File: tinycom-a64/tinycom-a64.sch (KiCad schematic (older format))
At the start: 25 parts, among them P1 CONN_02X10, P2 CONN_02X10, U1 AllWinner-A64(FBGA396), U2 H5TQG63BFR/FBGA96

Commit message: route
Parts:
- added C? (x2): C_Small, Capacitors_SMD:C_0603, symbol C_Small
- added Y1: Crystal, Crystals:crystal_FA238-TSX3225, symbol Crystal
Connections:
- net GND: now also C?.2, C?.2
- net SDC0_CLK: now also U1.AC8 (PF2/SDC0-CLK/UART0-TX)
- net SDC0_CMD: now also U1.W9 (PF3/SDC0-CMD/JTAG-DO1)
- net SDC0_D0: now also U1.W13 (PF1/SDC0-D0/JTAG-DI1)
- net SDC0_D1: now also U1.AB10 (PF0/SDC0-D1/JTAG-MS1)
- net SDC0_D2: now also U1.AB9 (PF5/SDC0-D2/JTAG-CK1)
- net SDC0_D3: now also U1.AB6 (PF4/SDC0-D3/UART0-RX)
- net UD0_N: now also U1.B22 (USB0-DM)
- net UD0_P: now also U1.A22 (USB0-DP)
- net UD2_N: now also U1.C22 (USB1-DM)
- net UD2_P: now also U1.B23 (USB1-DP)
- net at U1.K22 (X24MI): now also C?.1, Y1.1
- net at U1.K23 (X24MO): now also C?.1, Y1.2
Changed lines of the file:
@@
 $EndComp
 $Comp
-L GND #PWR4
+L GND #PWR01
 U 1 1 563E445F
 P 17800 6150
-F 0 "#PWR4" H 17800 5900 50  0001 C CNN
+F 0 "#PWR01" H 17800 5900 50  0001 C CNN
 F 1 "GND" H 17800 6000 50  0000 C CNN
 F 2 "" H 17800 6150 60  0000 C CNN
@@
 SCK_P
 $Comp
-L GND #PWR3
+L GND #PWR02
 U 1 1 563ECE56
 P 14950 850
-F 0 "#PWR3" H 14950 600 50  0001 C CNN
+F 0 "#PWR02" H 14950 600 50  0001 C CNN
 F 1 "GND" H 14950 700 50  0000 C CNN
 F 2 "" H 14950 850 60  0000 C CNN
@@
 $EndComp
 $Comp
-L GND #PWR1
+L GND #PWR03
 U 1 1 563EDF36
 P 13600 5900
-F 0 "#PWR1" H 13600 5650 50  0001 C CNN
+F 0 "#PWR03" H 13600 5650 50  0001 C CNN
 F 1 "GND" H 13600 5750 50  0000 C CNN
 F 2 "" H 13600 5900 60  0000 C CNN
@@
 $EndComp
 $Comp
-L GND #PWR2
+L GND #PWR04
 U 1 1 563EE398
 P 14350 5150
-F 0 "#PWR2" H 14350 4900 50  0001 C CNN
+F 0 "#PWR04" H 14350 4900 50  0001 C CNN
 F 1 "GND" H 14350 5000 50  0000 C CNN
 F 2 "" H 14350 5150 60  0000 C CNN
@@
 VCC_33
 $Comp
-L GND #PWR5
+L GND #PWR05
 U 1 1 56440C85
 P 19500 8700
-F 0 "#PWR5" H 19500 8450 50  0001 C CNN
+F 0 "#PWR05" H 19500 8450 50  0001 C CNN
 F 1 "GND" H 19500 8550 50  0000 C CNN
 F 2 "" H 19500 8700 60  0000 C CNN
@@
 $EndComp
 $Comp
-L GND #PWR7
+L GND #PWR06
 U 1 1 56441E51
 P 20300 8700
-F 0 "#PWR7" H 20300 8450 50  0001 C CNN
+F 0 "#PWR06" H 20300 8450 50  0001 C CNN
 F 1 "GND" H 20300 8550 50  0000 C CNN
 F 2 "" H 20300 8700 60  0000 C CNN
@@
 $EndComp
 $Comp
-L GND #PWR9
+L GND #PWR07
 U 1 1 564426D1
 P 20950 8700
-F 0 "#PWR9" H 20950 8450 50  0001 C CNN
+F 0 "#PWR07" H 20950 8450 50  0001 C CNN
 F 1 "GND" H 20950 8550 50  0000 C CNN
 F 2 "" H 20950 8700 60  0000 C CNN
@@
 HSDA
 $Comp
-L GND #PWR6
+L GND #PWR08
 U 1 1 56627185
 P 19800 9450
-F 0 "#PWR6" H 19800 9200 50  0001 C CNN
+F 0 "#PWR08" H 19800 9200 50  0001 C CNN
 F 1 "GND" H 19800 9300 50  0000 C CNN
 F 2 "" H 19800 9450 50  0000 C CNN
@@
 UART0_TX
 $Comp
-L GND #PWR8
+L GND #PWR09
 U 1 1 566278FC
 P 20500 10550
-F 0 "#PWR8" H 20500 10300 50  0001 C CNN
+F 0 "#PWR09" H 20500 10300 50  0001 C CNN
 F 1 "GND" H 20500 10400 50  0000 C CNN
 F 2 "" H 20500 10550 50  0000 C CNN
@@
 Text GLabel 11450 6250 2    60   Input ~ 0
 SVREF
+Text GLabel 7950 1800 2    60   Input ~ 0
+SDC0_D1
+Text GLabel 7950 1900 2    60   Input ~ 0
+SDC0_D0
+Text GLabel 7950 2000 2    60   Input ~ 0
+SDC0_CLK
+Text GLabel 7950 2100 2    60   Input ~ 0
+SDC0_CMD
+Text GLabel 7950 2200 2    60   Input ~ 0
+SDC0_D3
+Text GLabel 7950 2300 2    60   Input ~ 0
+SDC0_D2
+Text GLabel 6350 7900 2    60   Input ~ 0
+UD0_N
+Text GLabel 6350 8000 2    60   Input ~ 0
+UD0_P
+Text GLabel 6350 8100 2    60   Input ~ 0
+UD2_N
+Text GLabel 6350 8200 2    60   Input ~ 0
+UD2_P
+Wire Wire Line
+	1650 2050 1650 2100
+Wire Wire Line
+	1050 1850 1450 1850
+Wire Wire Line
+	1450 1850 1450 2000
+Wire Wire Line
+	1450 2000 1650 2000
+$Comp
+L Crystal Y1
+U 1 1 5669666E
+P 1200 2050
+F 0 "Y1" H 1200 2200 50  0000 C CNN
+F 1 "Crystal" H 1200 1900 50  0000 C CNN
+F 2 "Crystals:crystal_FA238-TSX3225" H 1200 2050 50  0000 C CNN
+F 3 "" H 1200 2050 50  0000 C CNN
+	1    1200 2050
+	-1   0    0    -1
+$EndComp
+Wire Wire Line
+	1650 2050 1350 2050
+Connection ~ 1050 2050
+Wire Wire Line
+	1350 2050 1350 2200
+Wire Wire Line
+	1050 1850 1050 2200
+$Comp
+L C_Small C?
+U 1 1 56694D06
+P 1050 2300
+F 0 "C?" H 1060 2370 50  0000 L CNN
+F 1 "C_Small" H 1060 2220 50  0000 L CNN
+F 2 "Capacitors_SMD:C_0603" H 1050 2300 60  0001 C CNN
+F 3 "" H 1050 2300 60  0000 C CNN
+	1    1050 2300
+	1    0    0    -1
+$EndComp
+$Comp
+L C_Small C?
+U 1 1 566951D3
+P 1350 2300
+F 0 "C?" H 1360 2370 50  0000 L CNN
+F 1 "C_Small" H 1360 2220 50  0000 L CNN
+F 2 "Capacitors_SMD:C_0603" H 1350 2300 60  0001 C CNN
+F 3 "" H 1350 2300 60  0000 C CNN
+	1    1350 2300
+	1    0    0    -1
+$EndComp
+$Comp
+L GND #PWR?
+U 1 1 5669523B
+P 1050 2400
+F 0 "#PWR?" H 1050 2150 50  0001 C CNN
+F 1 "GND" H 1050 2250 50  0000 C CNN
+F 2 "" H 1050 2400 50  0000 C CNN
+F 3 "" H 1050 2400 50  0000 C CNN
+	1    1050 2400
+	1    0    0    -1
+$EndComp
+$Comp
+L GND #PWR?
+U 1 1 566952BF
+P 1350 2400
+F 0 "#PWR?" H 1350 2150 50  0001 C CNN
+F 1 "GND" H 1350 2250 50  0000 C CNN
+F 2 "" H 1350 2400 50  0000 C CNN
+F 3 "" H 1350 2400 50  0000 C CNN
+	1    1350 2400
+	1    0    0    -1
+$EndComp
 $EndSCHEMATC

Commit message: xxx
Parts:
- gave numbers to parts that had none: 2
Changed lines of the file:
@@
 $EndComp
 $Comp
-L GND #PWR01
+L GND #PWR6
 U 1 1 563E445F
 P 17800 6150
-F 0 "#PWR01" H 17800 5900 50  0001 C CNN
+F 0 "#PWR6" H 17800 5900 50  0001 C CNN
 F 1 "GND" H 17800 6000 50  0000 C CNN
 F 2 "" H 17800 6150 60  0000 C CNN
@@
 SCK_P
 $Comp
-L GND #PWR02
+L GND #PWR5
 U 1 1 563ECE56
 P 14950 850
-F 0 "#PWR02" H 14950 600 50  0001 C CNN
+F 0 "#PWR5" H 14950 600 50  0001 C CNN
 F 1 "GND" H 14950 700 50  0000 C CNN
 F 2 "" H 14950 850 60  0000 C CNN
@@
 $EndComp
 $Comp
-L GND #PWR03
+L GND #PWR3
 U 1 1 563EDF36
 P 13600 5900
-F 0 "#PWR03" H 13600 5650 50  0001 C CNN
+F 0 "#PWR3" H 13600 5650 50  0001 C CNN
 F 1 "GND" H 13600 5750 50  0000 C CNN
 F 2 "" H 13600 5900 60  0000 C CNN
@@
 $EndComp
 $Comp
-L GND #PWR04
+L GND #PWR4
 U 1 1 563EE398
 P 14350 5150
-F 0 "#PWR04" H 14350 4900 50  0001 C CNN
+F 0 "#PWR4" H 14350 4900 50  0001 C CNN
 F 1 "GND" H 14350 5000 50  0000 C CNN
 F 2 "" H 14350 5150 60  0000 C CNN
@@
 VCC_33
 $Comp
-L GND #PWR05
+L GND #PWR7
 U 1 1 56440C85
 P 19500 8700
-F 0 "#PWR05" H 19500 8450 50  0001 C CNN
+F 0 "#PWR7" H 19500 8450 50  0001 C CNN
 F 1 "GND" H 19500 8550 50  0000 C CNN
 F 2 "" H 19500 8700 60  0000 C CNN
@@
 $EndComp
 $Comp
-L GND #PWR06
+L GND #PWR9
 U 1 1 56441E51
 P 20300 8700
-F 0 "#PWR06" H 20300 8450 50  0001 C CNN
+F 0 "#PWR9" H 20300 8450 50  0001 C CNN
 F 1 "GND" H 20300 8550 50  0000 C CNN
 F 2 "" H 20300 8700 60  0000 C CNN
@@
 $EndComp
 $Comp
-L GND #PWR07
+L GND #PWR11
 U 1 1 564426D1
 P 20950 8700
-F 0 "#PWR07" H 20950 8450 50  0001 C CNN
+F 0 "#PWR11" H 20950 8450 50  0001 C CNN
 F 1 "GND" H 20950 8550 50  0000 C CNN
 F 2 "" H 20950 8700 60  0000 C CNN
@@
 HSDA
 $Comp
-L GND #PWR08
+L GND #PWR8
 U 1 1 56627185
 P 19800 9450
-F 0 "#PWR08" H 19800 9200 50  0001 C CNN
+F 0 "#PWR8" H 19800 9200 50  0001 C CNN
 F 1 "GND" H 19800 9300 50  0000 C CNN
 F 2 "" H 19800 9450 50  0000 C CNN
@@
 UART0_TX
 $Comp
-L GND #PWR09
+L GND #PWR10
 U 1 1 566278FC
 P 20500 10550
-F 0 "#PWR09" H 20500 10300 50  0001 C CNN
+F 0 "#PWR10" H 20500 10300 50  0001 C CNN
 F 1 "GND" H 20500 10400 50  0000 C CNN
 F 2 "" H 20500 10550 50  0000 C CNN
@@
 	1050 1850 1050 2200
 $Comp
-L C_Small C?
+L C_Small C1
 U 1 1 56694D06
 P 1050 2300
-F 0 "C?" H 1060 2370 50  0000 L CNN
+F 0 "C1" H 1060 2370 50  0000 L CNN
 F 1 "C_Small" H 1060 2220 50  0000 L CNN
 F 2 "Capacitors_SMD:C_0603" H 1050 2300 60  0001 C CNN
@@
 $EndComp
 $Comp
-L C_Small C?
+L C_Small C2
 U 1 1 566951D3
 P 1350 2300
-F 0 "C?" H 1360 2370 50  0000 L CNN
+F 0 "C2" H 1360 2370 50  0000 L CNN
 F 1 "C_Small" H 1360 2220 50  0000 L CNN
 F 2 "Capacitors_SMD:C_0603" H 1350 2300 60  0001 C CNN
@@
 $EndComp
 $Comp
-L GND #PWR?
+L GND #PWR1
 U 1 1 5669523B
 P 1050 2400
-F 0 "#PWR?" H 1050 2150 50  0001 C CNN
+F 0 "#PWR1" H 1050 2150 50  0001 C CNN
 F 1 "GND" H 1050 2250 50  0000 C CNN
 F 2 "" H 1050 2400 50  0000 C CNN
@@
 $EndComp
 $Comp
-L GND #PWR?
+L GND #PWR2
 U 1 1 566952BF
 P 1350 2400
-F 0 "#PWR?" H 1350 2150 50  0001 C CNN
+F 0 "#PWR2" H 1350 2150 50  0001 C CNN
 F 1 "GND" H 1350 2250 50  0000 C CNN
 F 2 "" H 1350 2400 50  0000 C CNN

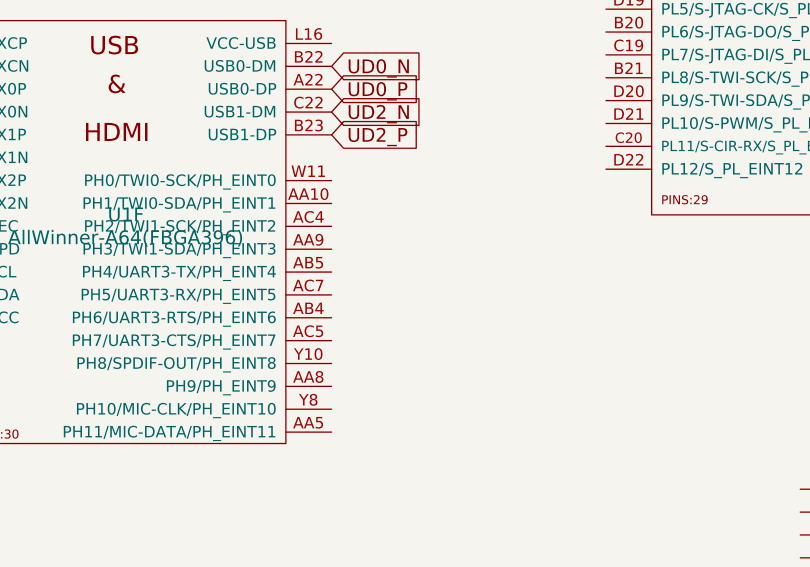
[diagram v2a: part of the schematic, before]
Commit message: route uart
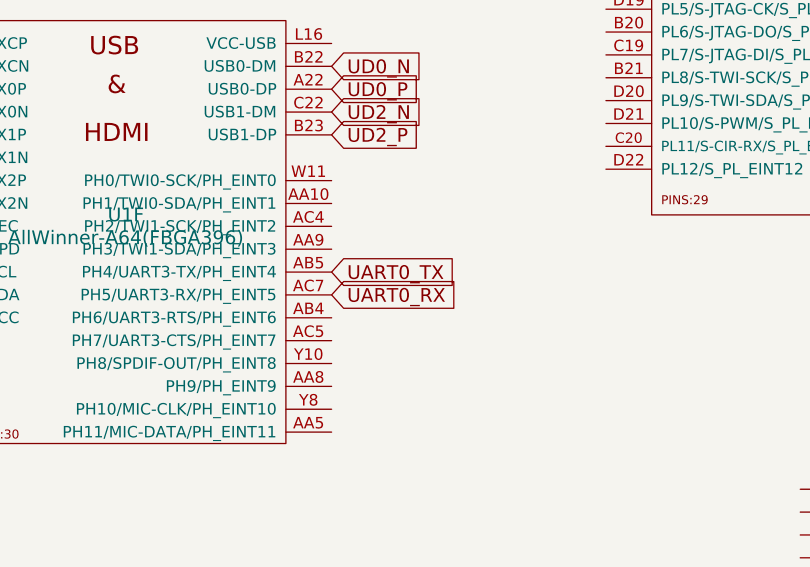
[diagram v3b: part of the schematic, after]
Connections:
- net UART0_RX: now also U1.AC7 (PH5/UART3-RX/PH_EINT5)
- net UART0_TX: now also U1.AB5 (PH4/UART3-TX/PH_EINT4)
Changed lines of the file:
@@
 $EndComp
 $Comp
-L GND #PWR6
+L GND #PWR01
 U 1 1 563E445F
 P 17800 6150
-F 0 "#PWR6" H 17800 5900 50  0001 C CNN
+F 0 "#PWR01" H 17800 5900 50  0001 C CNN
 F 1 "GND" H 17800 6000 50  0000 C CNN
 F 2 "" H 17800 6150 60  0000 C CNN
@@
 SCK_P
 $Comp
-L GND #PWR5
+L GND #PWR02
 U 1 1 563ECE56
 P 14950 850
-F 0 "#PWR5" H 14950 600 50  0001 C CNN
+F 0 "#PWR02" H 14950 600 50  0001 C CNN
 F 1 "GND" H 14950 700 50  0000 C CNN
 F 2 "" H 14950 850 60  0000 C CNN
@@
 $EndComp
 $Comp
-L GND #PWR3
+L GND #PWR03
 U 1 1 563EDF36
 P 13600 5900
-F 0 "#PWR3" H 13600 5650 50  0001 C CNN
+F 0 "#PWR03" H 13600 5650 50  0001 C CNN
 F 1 "GND" H 13600 5750 50  0000 C CNN
 F 2 "" H 13600 5900 60  0000 C CNN
@@
 $EndComp
 $Comp
-L GND #PWR4
+L GND #PWR04
 U 1 1 563EE398
 P 14350 5150
-F 0 "#PWR4" H 14350 4900 50  0001 C CNN
+F 0 "#PWR04" H 14350 4900 50  0001 C CNN
 F 1 "GND" H 14350 5000 50  0000 C CNN
 F 2 "" H 14350 5150 60  0000 C CNN
@@
 VCC_33
 $Comp
-L GND #PWR7
+L GND #PWR05
 U 1 1 56440C85
 P 19500 8700
-F 0 "#PWR7" H 19500 8450 50  0001 C CNN
+F 0 "#PWR05" H 19500 8450 50  0001 C CNN
 F 1 "GND" H 19500 8550 50  0000 C CNN
 F 2 "" H 19500 8700 60  0000 C CNN
@@
 $EndComp
 $Comp
-L GND #PWR9
+L GND #PWR06
 U 1 1 56441E51
 P 20300 8700
-F 0 "#PWR9" H 20300 8450 50  0001 C CNN
+F 0 "#PWR06" H 20300 8450 50  0001 C CNN
 F 1 "GND" H 20300 8550 50  0000 C CNN
 F 2 "" H 20300 8700 60  0000 C CNN
@@
 $EndComp
 $Comp
-L GND #PWR11
+L GND #PWR07
 U 1 1 564426D1
 P 20950 8700
-F 0 "#PWR11" H 20950 8450 50  0001 C CNN
+F 0 "#PWR07" H 20950 8450 50  0001 C CNN
 F 1 "GND" H 20950 8550 50  0000 C CNN
 F 2 "" H 20950 8700 60  0000 C CNN
@@
 HSDA
 $Comp
-L GND #PWR8
+L GND #PWR08
 U 1 1 56627185
 P 19800 9450
-F 0 "#PWR8" H 19800 9200 50  0001 C CNN
+F 0 "#PWR08" H 19800 9200 50  0001 C CNN
 F 1 "GND" H 19800 9300 50  0000 C CNN
 F 2 "" H 19800 9450 50  0000 C CNN
@@
 UART0_TX
 $Comp
-L GND #PWR10
+L GND #PWR09
 U 1 1 566278FC
 P 20500 10550
-F 0 "#PWR10" H 20500 10300 50  0001 C CNN
+F 0 "#PWR09" H 20500 10300 50  0001 C CNN
 F 1 "GND" H 20500 10400 50  0000 C CNN
 F 2 "" H 20500 10550 50  0000 C CNN
@@
 $EndComp
 $Comp
-L GND #PWR1
+L GND #PWR010
 U 1 1 5669523B
 P 1050 2400
-F 0 "#PWR1" H 1050 2150 50  0001 C CNN
+F 0 "#PWR010" H 1050 2150 50  0001 C CNN
 F 1 "GND" H 1050 2250 50  0000 C CNN
 F 2 "" H 1050 2400 50  0000 C CNN
@@
 $EndComp
 $Comp
-L GND #PWR2
+L GND #PWR011
 U 1 1 566952BF
 P 1350 2400
-F 0 "#PWR2" H 1350 2150 50  0001 C CNN
+F 0 "#PWR011" H 1350 2150 50  0001 C CNN
 F 1 "GND" H 1350 2250 50  0000 C CNN
 F 2 "" H 1350 2400 50  0000 C CNN
@@
 	1    0    0    -1
 $EndComp
+Text GLabel 6350 8800 2    60   Input ~ 0
+UART0_TX
+Text GLabel 6350 8900 2    60   Input ~ 0
+UART0_RX
 $EndSCHEMATC

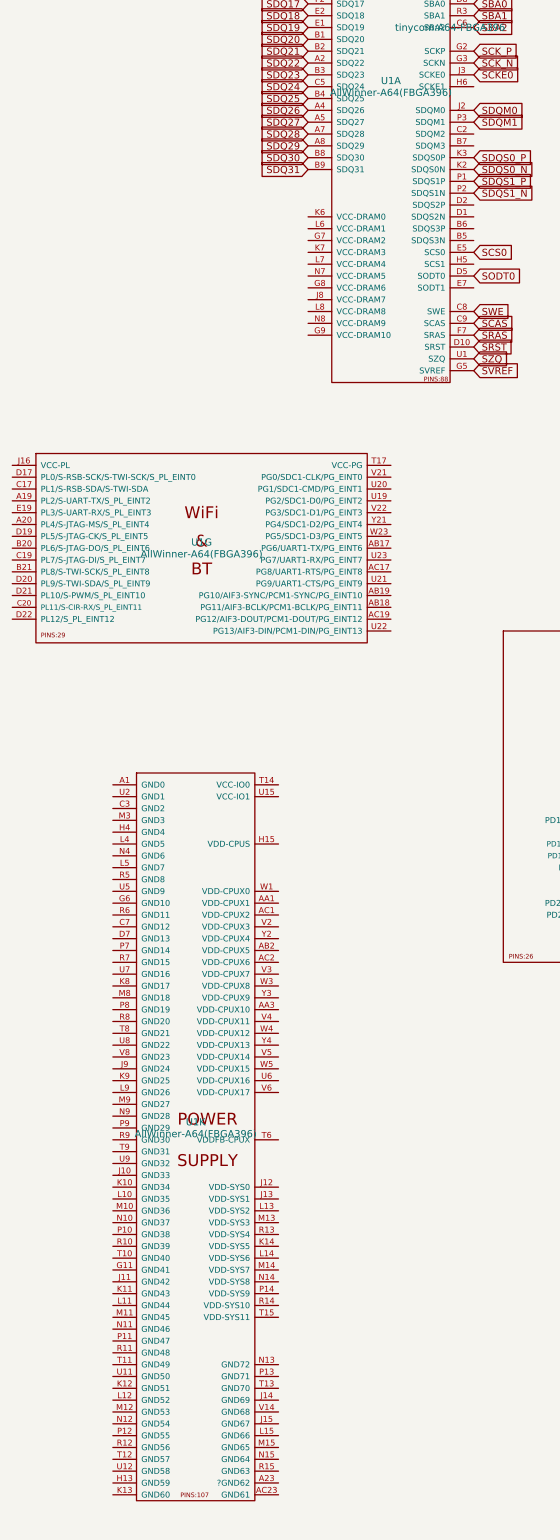
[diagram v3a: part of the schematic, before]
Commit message: route ddr power
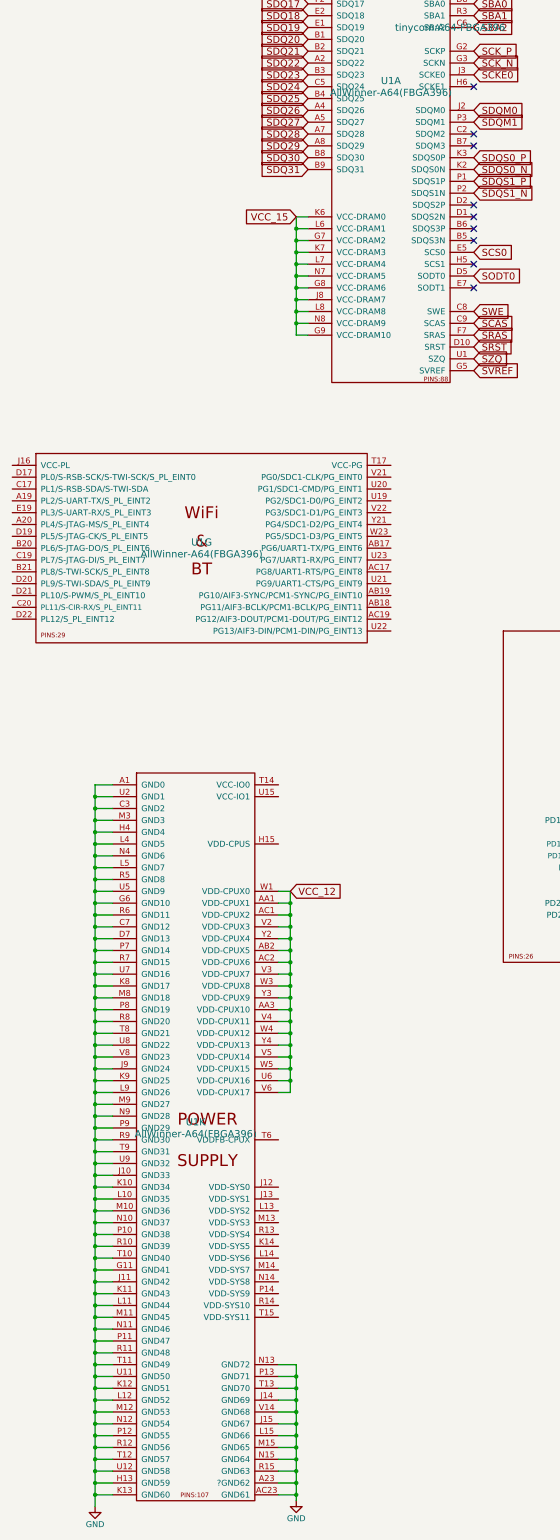
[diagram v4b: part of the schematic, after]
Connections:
- net GND: now also U1.A1 (GND0), U1.A23 (?GND62), U1.AC23 (GND61), U1.C3 (GND2), U1.C7 (GND12), U1.D7 (GND13), U1.G11 (GND41), U1.G6 (GND10), U1.H13 (GND59), U1.H4 (GND4), U1.J10 (GND33), U1.J11 (GND42), U1.J14 (GND69), U1.J15 (GND67), U1.J9 (GND24), U1.K10 (GND34), U1.K11 (GND43), U1.K12 (GND51), U1.K13 (GND60), U1.K8 (GND17), U1.K9 (GND25), U1.L10 (GND35), U1.L11 (GND44), U1.L12 (GND52), U1.L15 (GND66), U1.L4 (GND5), U1.L5 (GND7), U1.L9 (GND26), U1.M10 (GND36), U1.M11 (GND45), U1.M12 (GND53), U1.M15 (GND65), U1.M3 (GND3), U1.M8 (GND18), U1.M9 (GND27), U1.N10 (GND37), U1.N11 (GND46), U1.N12 (GND54), U1.N13 (GND72), U1.N15 (GND64), U1.N4 (GND6), U1.N9 (GND28), U1.P10 (GND38), U1.P11 (GND47), U1.P12 (GND55), U1.P13 (GND71), U1.P7 (GND14), U1.P8 (GND19), U1.P9 (GND29), U1.R10 (GND39), U1.R11 (GND48), U1.R12 (GND56), U1.R15 (GND63), U1.R5 (GND8), U1.R6 (GND11), U1.R7 (GND15), U1.R8 (GND20), U1.R9 (GND30), U1.T10 (GND40), U1.T11 (GND49), U1.T12 (GND57), U1.T13 (GND70), U1.T8 (GND21), U1.T9 (GND31), U1.U11 (GND50), U1.U12 (GND58), U1.U2 (GND1), U1.U5 (GND9), U1.U7 (GND16), U1.U8 (GND22), U1.U9 (GND32), U1.V14 (GND68), U1.V8 (GND23)
- net VCC_12: now also U1.AA1 (VDD-CPUX1), U1.AA3 (VDD-CPUX10), U1.AB2 (VDD-CPUX5), U1.AC1 (VDD-CPUX2), U1.AC2 (VDD-CPUX6), U1.U6 (VDD-CPUX16), U1.V2 (VDD-CPUX3), U1.V3 (VDD-CPUX7), U1.V4 (VDD-CPUX11), U1.V5 (VDD-CPUX14), U1.V6 (VDD-CPUX17), U1.W1 (VDD-CPUX0), U1.W3 (VDD-CPUX8), U1.W4 (VDD-CPUX12), U1.W5 (VDD-CPUX15), U1.Y2 (VDD-CPUX4), U1.Y3 (VDD-CPUX9), U1.Y4 (VDD-CPUX13)
- net VCC_15: now also U1.G7 (VCC-DRAM2), U1.G8 (VCC-DRAM6), U1.G9 (VCC-DRAM10), U1.J8 (VCC-DRAM7), U1.K6 (VCC-DRAM0), U1.K7 (VCC-DRAM3), U1.L6 (VCC-DRAM1), U1.L7 (VCC-DRAM4), U1.L8 (VCC-DRAM8), U1.N7 (VCC-DRAM5), U1.N8 (VCC-DRAM9)
- no-connect marks 5 -> 14

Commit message: route
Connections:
- net VCC_12: now also U1.J12 (VDD-SYS0), U1.J13 (VDD-SYS1), U1.K14 (VDD-SYS5), U1.L13 (VDD-SYS2), U1.L14 (VDD-SYS6), U1.M13 (VDD-SYS3), U1.M14 (VDD-SYS7), U1.N14 (VDD-SYS8), U1.P14 (VDD-SYS9), U1.R13 (VDD-SYS4), U1.R14 (VDD-SYS10), U1.T15 (VDD-SYS11)
- net VCC_33: now also U1.L16 (VCC-USB)
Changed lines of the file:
@@
 UART0_RX
 $Comp
-L GND #PWR?
+L GND #PWR012
 U 1 1 56696AA6
 P 8250 15850
-F 0 "#PWR?" H 8250 15600 50  0001 C CNN
+F 0 "#PWR012" H 8250 15600 50  0001 C CNN
 F 1 "GND" H 8250 15700 50  0000 C CNN
 F 2 "" H 8250 15850 50  0000 C CNN
@@
 Connection ~ 9900 12250
 $Comp
-L GND #PWR?
+L GND #PWR013
 U 1 1 5669EC55
 P 9950 15800
-F 0 "#PWR?" H 9950 15550 50  0001 C CNN
+F 0 "#PWR013" H 9950 15550 50  0001 C CNN
 F 1 "GND" H 9950 15650 50  0000 C CNN
 F 2 "" H 9950 15800 50  0000 C CNN
@@
 NoConn ~ 11450 5350
 NoConn ~ 11450 5550
+Wire Wire Line
+	9800 13150 9900 13150
+Wire Wire Line
+	9900 13150 9900 14250
+Wire Wire Line
+	9900 14250 9800 14250
+Wire Wire Line
+	9800 13250 9900 13250
+Connection ~ 9900 13250
+Wire Wire Line
+	9800 13350 9900 13350
+Connection ~ 9900 13350
+Wire Wire Line
+	9800 13450 9900 13450
+Connection ~ 9900 13450
+Wire Wire Line
+	9800 13550 9900 13550
+Connection ~ 9900 13550
+Wire Wire Line
+	9800 13650 9900 13650
+Connection ~ 9900 13650
+Wire Wire Line
+	9800 13750 9900 13750
+Connection ~ 9900 13750
+Wire Wire Line
+	9800 13850 9900 13850
+Connection ~ 9900 13850
+Wire Wire Line
+	9800 13950 9900 13950
+Connection ~ 9900 13950
+Wire Wire Line
+	9800 14050 9900 14050
+Connection ~ 9900 14050
+Wire Wire Line
+	9800 14150 9900 14150
+Connection ~ 9900 14150
+Text GLabel 9900 13150 2    60   Input ~ 0
+VCC_12
+Text GLabel 6350 7800 2    60   Input ~ 0
+VCC_33
 $EndSCHEMATC

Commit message: reroute, escape bga
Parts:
- C1, C2: value C_Small -> 33pF
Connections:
- net VCC_12 is gone; now on net VCC_11: C14.1, C15.1, C20.1, C22.1, C6.1, P2.3 (P3), U1.AA1 (VDD-CPUX1), U1.AA3 (VDD-CPUX10), U1.AB2 (VDD-CPUX5), U1.AC1 (VDD-CPUX2), U1.AC2 (VDD-CPUX6), U1.J12 (VDD-SYS0), U1.J13 (VDD-SYS1), U1.K14 (VDD-SYS5), U1.L13 (VDD-SYS2), U1.L14 (VDD-SYS6), U1.M13 (VDD-SYS3), U1.M14 (VDD-SYS7), U1.N14 (VDD-SYS8), U1.P14 (VDD-SYS9), U1.R13 (VDD-SYS4), U1.R14 (VDD-SYS10), U1.T15 (VDD-SYS11), U1.U6 (VDD-CPUX16), U1.V2 (VDD-CPUX3), U1.V3 (VDD-CPUX7), U1.V4 (VDD-CPUX11), U1.V5 (VDD-CPUX14), U1.V6 (VDD-CPUX17), U1.W1 (VDD-CPUX0), U1.W3 (VDD-CPUX8), U1.W4 (VDD-CPUX12), U1.W5 (VDD-CPUX15), U1.Y2 (VDD-CPUX4), U1.Y3 (VDD-CPUX9), U1.Y4 (VDD-CPUX13)
- net VCC_30: now also U1.G14 (AVCC), U1.H16 (VCC-RTC), U1.N16 (VCC-PLL)
- net VCC_33: now also U1.J16 (VCC-PL), U1.M16 (HVCC), U1.N18 (VCC-EFUSE), U1.N19 (VCC-DSI), U1.R16 (VCC-PC), U1.T14 (VCC-IO0), U1.T17 (VCC-PG), U1.U15 (VCC-IO1), U1.U16 (VCC-PD), U1.U18 (VCC-PE)
- net VCC_11: now reaches U1.K16 (HSIC-VCC)
- net VCC_11: now also U1.H15 (VDD-CPUS)
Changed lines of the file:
@@
 $EndComp
 Text GLabel 20300 8100 0    60   Input ~ 0
-VCC_12
+VCC_11
 $Comp
 L C_Small C6
@@
 VCC_33
 Text GLabel 20650 9700 0    60   Input ~ 0
-VCC_12
+VCC_11
 Text GLabel 20650 9800 0    60   Input ~ 0
 VCC_15
@@
 P 1050 2300
 F 0 "C1" H 1060 2370 50  0000 L CNN
-F 1 "C_Small" H 1060 2220 50  0000 L CNN
+F 1 "33pF" H 1060 2220 50  0000 L CNN
 F 2 "Capacitors_SMD:C_0603" H 1050 2300 60  0001 C CNN
 F 3 "" H 1050 2300 60  0000 C CNN
@@
 P 1350 2300
 F 0 "C2" H 1360 2370 50  0000 L CNN
-F 1 "C_Small" H 1360 2220 50  0000 L CNN
+F 1 "33pF" H 1360 2220 50  0000 L CNN
 F 2 "Capacitors_SMD:C_0603" H 1350 2300 60  0001 C CNN
 F 3 "" H 1350 2300 60  0000 C CNN
@@
 	9900 10650 9800 10650
 Text GLabel 9900 10650 2    60   Input ~ 0
-VCC_12
+VCC_11
 Wire Wire Line
 	9800 10750 9900 10750
@@
 Connection ~ 9900 14150
 Text GLabel 9900 13150 2    60   Input ~ 0
-VCC_12
+VCC_11
 Text GLabel 6350 7800 2    60   Input ~ 0
 VCC_33
+Text GLabel 4550 9000 0    60   Input ~ 0
+VCC_33
+Text GLabel 1600 13050 0    60   Input ~ 0
+VCC_33
+Text GLabel 1600 13150 0    60   Input ~ 0
+VCC_33
+Text GLabel 14100 8550 2    60   Input ~ 0
+VCC_33
+Text GLabel 10750 7050 2    60   Input ~ 0
+VCC_33
+Text GLabel 7550 7050 0    60   Input ~ 0
+VCC_33
+Text GLabel 5550 1950 2    60   Input ~ 0
+VCC_33
+Text GLabel 3050 1700 2    60   Input ~ 0
+VCC_11
+Text GLabel 3050 2100 2    60   Input ~ 0
+VCC_33
+Text GLabel 3050 2400 2    60   Input ~ 0
+VCC_30
+Text GLabel 3050 2700 2    60   Input ~ 0
+VCC_30
+Text GLabel 1500 7950 0    60   Input ~ 0
+VCC_30
+Text GLabel 9800 10250 2    60   Input ~ 0
+VCC_11
+Wire Wire Line
+	9800 9750 9900 9750
+Wire Wire Line
+	9900 9750 9900 9850
+Wire Wire Line
+	9900 9850 9800 9850
+Text GLabel 9900 9750 2    60   Input ~ 0
+VCC_33
 $EndSCHEMATC
